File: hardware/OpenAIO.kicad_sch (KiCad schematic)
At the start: 5 parts, among them J1 OpenDrone-Core, U24 AIO_outline, U25 INA186A3IDCKR

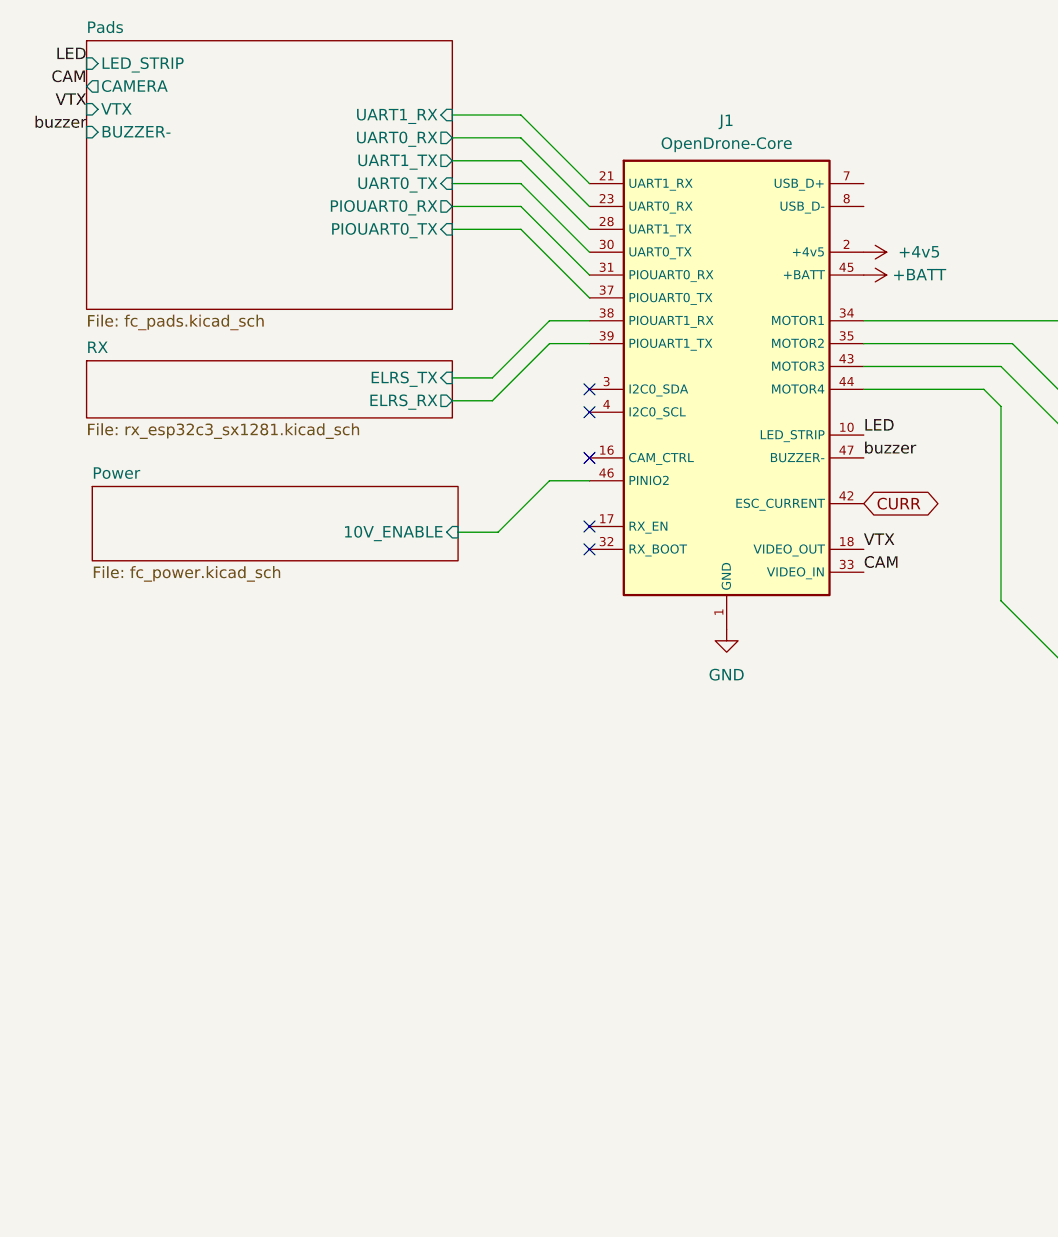
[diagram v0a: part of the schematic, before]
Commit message: Type-C front end back on the root, missing parts placed on the board
Root sheet: USB1, R3, R4 and their power flags redrawn after the core swap.
Board: C25, C27, D7, R23 and J35 to J55 placed, Card1, R34 and C36 removed,
24 of the stubs left at the old J90 pads cleaned up.
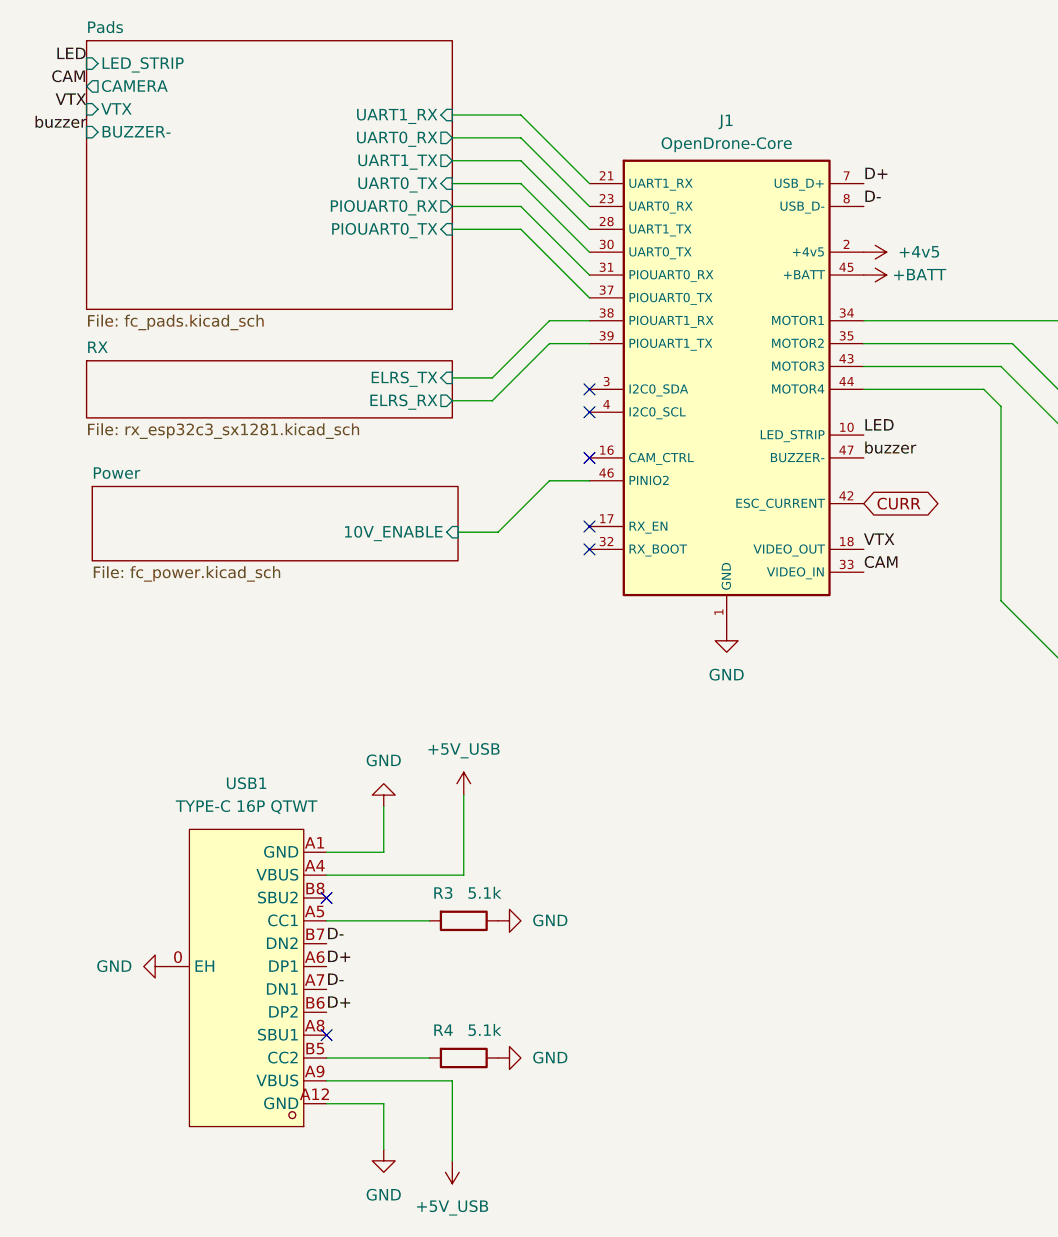
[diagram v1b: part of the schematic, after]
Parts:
- added R3, R4: 5.1k, Resistor_SMD:R_0201_0603Metric, symbol Device:R
- added USB1: TYPE-C 16P QTWT, lib:USB-TYPE-C-SMD_TYPE-C-16P-QTWT, symbol lib:TYPE-C16PQTWT
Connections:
- net GND: now also R3.1, R4.1, USB1.0 (EH), USB1.A1 (GND), USB1.A12 (GND)
- net D+: now reaches J1.7 (USB_D+)
- net D+: now also USB1.A6 (DP1), USB1.B6 (DP2)
- net D-: now reaches J1.8 (USB_D-)
- net D-: now also USB1.A7 (DN1), USB1.B7 (DN2)
- new net: R3.2, USB1.A5 (CC1)
- new net: R4.2, USB1.B5 (CC2)
- new net +5V_USB: USB1.A4 (VBUS), USB1.A9 (VBUS)
- no-connect marks 5 -> 7

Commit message: chore: consolidate OpenAIO design assets and guidance
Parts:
- removed C104: 100nF, Capacitor_SMD:C_0201_0603Metric, symbol ESCLibrary:GRM033R61C104KE84D
- removed U25: INA186A3IDCKR, 4in1ESC:SOT-363_SC-70-6, symbol components:INA186A3IDCKR
- added C83, C85: 100nF, Capacitor_SMD:C_0402_WIDE, symbol ESCLibrary:GRM033R61C104KE84D
- added C84: 1uF, Capacitor_SMD:C_0402_1005Metric, symbol ESCLibrary:GRM033R61C104KE84D
- added C93, C94: 100nF, Capacitor_SMD:C_0201_0603Metric, symbol ESCLibrary:GRM033R61C104KE84D
- added R93, R94: 1k, Capacitor_SMD:C_0201_0603Metric, symbol components:0201_1kR
- added R95: 1k, 4in1ESC:R_0201_0603Metric, symbol ESCLibrary:0201_1kR
- added U19: INA186A3IDCKR, 4in1ESC:SOT-363_SC-70-6, symbol components:INA186A3IDCKR
- Rsense2: KiLib_Generator SMD_2terminal_chip_molded -> (none); Manufacturer (none) -> Yezhan
- renumbered R3 to R1, R4 to R2, U24 to U1
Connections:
- net RX/ELRS_RX is gone; now on net Pads/UART1_TX: J1.39 (PIOUART0_RX)
- net RX/ELRS_TX is gone; now on net GND: J1.38 (GND)
- net +3V3: now also C93.1, U19.3 (VS)
- net +4v5: now also J1.3 (+4v5); no longer J1.2 (+4v5)
- net +BATT: now also J1.7 (+BATT), R93.2; no longer J1.45 (+BATT)
- net CAM: now also J1.30 (VIDEO_IN); no longer J1.33 (VIDEO_IN)
- net CSA+: now also R94.2
- net CURR: now also J1.2 (ESC_CURRENT), C94.1, R95.1; no longer J1.42 (ESC_CURRENT)
- net D+: now also J1.15 (D-); no longer J1.7 (USB_D+)
- net D-: now also J1.22 (D+); no longer J1.8 (USB_D-)
- net ESC1/dshot: now also J1.8 (MOTOR1); no longer J1.34 (MOTOR1)
- net ESC2/dshot: now also J1.9 (MOTOR2); no longer J1.35 (MOTOR2)
- net ESC3/dshot: now also J1.10 (MOTOR3); no longer J1.43 (MOTOR3)
- net ESC4/dshot: now also J1.11 (MOTOR4); no longer J1.44 (MOTOR4)
- net GND: now also J1.16 (GND), J1.17 (GND), J1.18 (GND), J1.21 (GND), J1.32 (GND), J1.33 (GND), J1.34 (GND), J1.35 (GND), J1.37 (GND), J1.4 (GND), J1.42 (GND), J1.43 (GND), J1.44 (GND), J1.46 (GND), J1.47 (GND), C83.2, C85.2, C93.2, C94.2, U19.1 (REF), U19.2 (GND); no longer J1.11 (GND), J1.12 (GND), J1.13 (GND), J1.15 (GND), J1.22 (GND), J1.24 (GND), J1.26 (GND), J1.29 (GND), J1.40 (GND), J1.48 (GND), J1.49 (GND), J1.50 (GND), J1.51 (GND), J1.52 (GND), J1.53 (GND), J1.54 (GND), J1.6 (GND), J1.9 (GND)
- net LED: now also J1.6 (LED_STRIP); no longer J1.10 (LED_STRIP)
- net Pads/PIOUART0_RX: now also J1.48 (UART0_TX); no longer J1.31 (PIOUART0_RX)
- net Pads/PIOUART0_TX: now also J1.49 (UART0_RX); no longer J1.37 (PIOUART0_TX)
- net Pads/UART0_RX: now also J1.31 (PIOUART1_TX); no longer J1.23 (UART0_RX)
- net Pads/UART0_TX: now also J1.40 (PIOUART0_TX); no longer J1.30 (UART0_TX)
- net Pads/UART1_RX: now also J1.26 (PIOUART1_RX); no longer J1.21 (UART1_RX)
- net Pads/UART1_TX: no longer J1.28 (UART1_TX)
- net Power/10V_ENABLE: now also J1.23 (10V_ENABLE); no longer J1.46 (PINIO2)
- net VTX: now also J1.45 (VIDEO_OUT); no longer J1.18 (VIDEO_OUT)
- net buzzer: now also J1.52 (BUZZER-); no longer J1.47 (BUZZER-)
- new net: C83.1, C84.1, R93.1, U19.5 (-IN)
- new net: C84.2, C85.1, R94.1, U19.4 (+IN)
- new net: R95.2, U19.6 (OUT)
- new net RX Mono/ELRS_BOOT: J1.28 (RX_BOOT)
- new net RX Mono/ELRS_EN: J1.29 (RX_EN)
- new net RX Mono/ELRS_RX: J1.51 (UART1_TX)
- new net RX Mono/ELRS_TX: J1.50 (UART1_RX)
- no-connect marks 7 -> 5
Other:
- removed sheet RX
- added sheet RX Mono (esp32c3_lr1121_mono.kicad_sch)
- moved on the sheet: R1, R2, U1, USB1
